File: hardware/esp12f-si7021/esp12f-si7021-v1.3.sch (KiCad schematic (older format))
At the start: 23 parts, among them J1 JST PH3, J2 ESP_01x06_Female, J3 JST PH2, J4 JST GH2, Q1 BSS84, U1 MCP1700-3302E_SOT23, U2 ESP-12F, U3 Si7021-A20

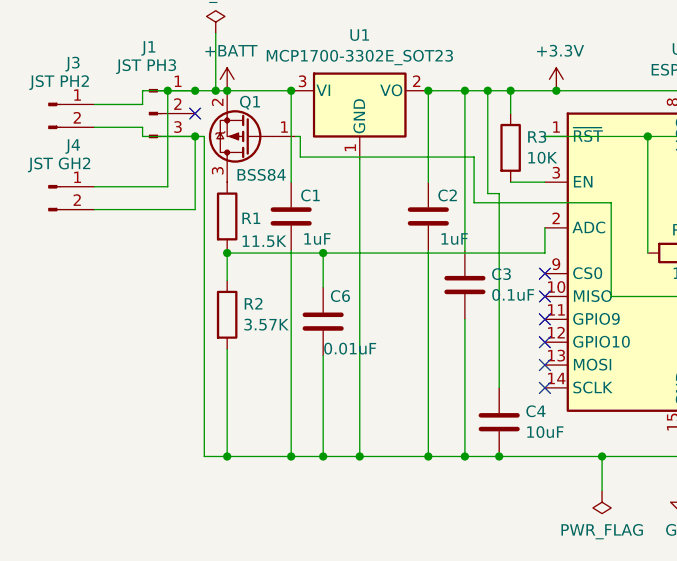
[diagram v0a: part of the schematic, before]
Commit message: Tweak resistor values
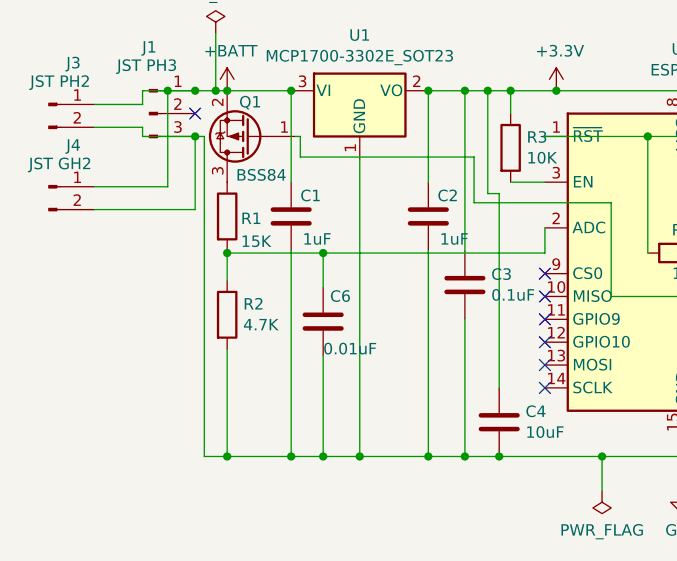
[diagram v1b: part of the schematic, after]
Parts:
- R1: value 11.5K -> 15K
- R2: value 3.57K -> 4.7K
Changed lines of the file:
@@
 P 4110 3480
 F 0 "R2" H 4180 3526 50  0000 L CNN
-F 1 "3.57K" H 4180 3435 50  0000 L CNN
+F 1 "4.7K" H 4180 3435 50  0000 L CNN
 F 2 "Resistor_SMD:R_1206_3216Metric_Pad1.30x1.75mm_HandSolder" V 4040 3480 50  0001 C CNN
 F 3 "~" H 4110 3480 50  0001 C CNN
@@
 P 4110 3050
 F 0 "R1" H 4170 3040 50  0000 L CNN
-F 1 "11.5K" H 4170 2940 50  0000 L CNN
+F 1 "15K" H 4170 2940 50  0000 L CNN
 F 2 "Resistor_SMD:R_1206_3216Metric_Pad1.30x1.75mm_HandSolder" V 4040 3050 50  0001 C CNN
 F 3 "~" H 4110 3050 50  0001 C CNN
